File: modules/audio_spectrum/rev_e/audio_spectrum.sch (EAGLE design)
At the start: 110 parts, among them J1 AUDIO-JACK-VERTICAL, J2 SIGNPOST_DEBUG_HEADER, J3 SIGNPOST_MODULE_HEADER, J4 TC2030-JLINK-L, P1 4k-200k, P2 4k-200k, Q1 NX3008PBK, Q2 NX3008PBK, U1 AT45DB641EUDFN, U10 TLV62130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

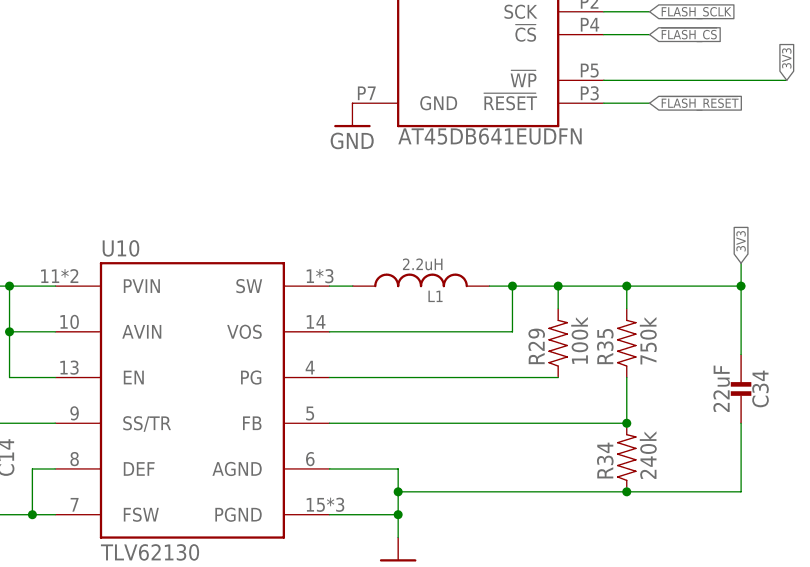
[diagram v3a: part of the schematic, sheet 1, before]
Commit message: added MPN, new BOM
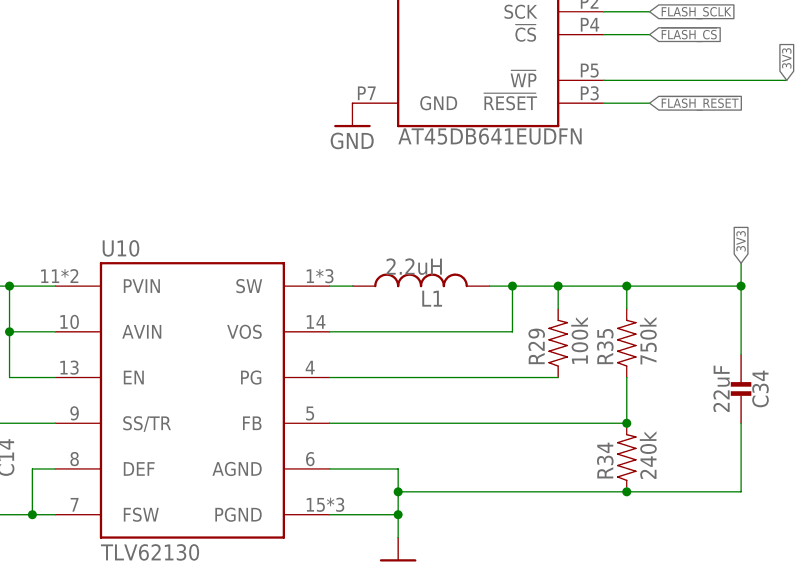
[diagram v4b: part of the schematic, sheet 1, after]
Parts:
- C1, C2: MANUFACTURER (none) -> Murata; MPN (none) -> GRM1555C1H8R0BA01D
- C10, C11, C9: MANUFACTURER (none) -> Murata; MPN (none) -> GRM188R71H102KA01D
- C12, C13: MANUFACTURER (none) -> Murata; MPN (none) -> GCM1885C1H122JA16D
- C14: MANUFACTURER (none) -> Murata; MPN (none) -> GRM188R71H332KA01D
- C15, C16, C17, C18, C19, C21, C22, C23, C24: MANUFACTURER (none) -> Murata; MPN (none) -> GRM188R71C104KA01D
- C20: MANUFACTURER (none) -> Murata; MPN (none) -> GRM155R71A104JA01D
- C25, C26, C27, C28, C29: MANUFACTURER (none) -> Murata; MPN (none) -> GRM188R61C105KA93D
- C3, C4: MANUFACTURER (none) -> Murata; MPN (none) -> GRM1885C1H330JA01D
- C30, C31: MANUFACTURER (none) -> Murata; MPN (none) -> GRM188R60J475KE19D
- C32: MANUFACTURER (none) -> TDk; MPN (none) -> C1608X5R1A685K080AC
- C33: MANUFACTURER (none) -> Murata; MPN (none) -> GRM188R60J106ME47J
- C34: MANUFACTURER (none) -> Murata; MPN (none) -> GRM186R60J226ME15D
- C5, C6: MANUFACTURER (none) -> Murata; MPN (none) -> GRM1885C1H101JA01D
- C7, C8: MANUFACTURER (none) -> Murata; MPN (none) -> GRM1885C1H361JA01D
- FB1: MANUFACTURER (none) -> Murata; MPN (none) -> BLM18HE152SN1D
- J1: MANUFACTURER (none) -> Kycon; MPN (none) -> STX-3790-5N
- L2: MANUFACTURER (none) -> Murata; MPN (none) -> LQH3NPN220MJ0L
- LED1, LED3: MANUFACTURER (none) -> Lite-On; MPN (none) -> LTST-C191KGKT
- LED2, LED4: MANUFACTURER (none) -> Lite-On; MPN (none) -> LTST-C191KRKT
- R1: MANUFACTURER (none) -> Samsung; MPN (none) -> RC1005F103CS
- R10, R11, R12, R13, R14: MANUFACTURER (none) -> Rohm; MPN (none) -> MCR03EZPFX1002
- R15, R16: MANUFACTURER (none) -> Rohm; MPN (none) -> MCR03ERTF1912
- R17, R18, R19, R20, R21, R22, R23, R24: MANUFACTURER (none) -> Rohm; MPN (none) -> MCR03ERTJ203
- R2, R3, R4, R5: MANUFACTURER (none) -> Murata; MPN (none) -> ESR03EZPJ102
- R25: MANUFACTURER (none) -> Rohm; MPN (none) -> MCR03ERTF6042
- R26, R27, R28, R29, R30, R31: MANUFACTURER (none) -> Rohm; MPN (none) -> MCR03ERTJ104
- R32, R33: MANUFACTURER (none) -> Rohm; MPN (none) -> MCR03ERTF2003
- R34: MANUFACTURER (none) -> Rohm; MPN (none) -> RHM240KCFCT-ND
- R35: MANUFACTURER (none) -> Rohm; MPN (none) -> MCR03ERTF7503
- R6, R7, R8, R9: MANUFACTURER (none) -> Rohm; MPN (none) -> MCR03ERTJ152

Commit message: changed data, added advref
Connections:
- net N$32: now also U9.ADVREFP
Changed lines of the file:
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@@
 <attribute name="DIGIKEY" value="RHM1.5KCGCT-ND"/>
 <attribute name="MANUFACTURER" value="Rohm"/>
-<attribute name="MPN" value="MCR03ERTJ152
-"/>
+<attribute name="MPN" value="MCR03ERTJ152 "/>
 </part>
 <part name="C30" library="passives" deviceset="CAPACITOR" device="0603_CAP" value="4.7uF">
@@
 <attribute name="DIGIKEY" value="RHM1.5KCGCT-ND"/>
 <attribute name="MANUFACTURER" value="Rohm"/>
-<attribute name="MPN" value="MCR03ERTJ152
-"/>
+<attribute name="MPN" value="MCR03ERTJ152 "/>
 </part>
 <part name="C31" library="passives" deviceset="CAPACITOR" device="0603_CAP" value="4.7uF">
@@
 <wire x1="119.38" y1="157.48" x2="91.44" y2="157.48" width="0.1524" layer="91"/>
 <junction x="91.44" y="157.48"/>
+<pinref part="U9" gate="U1" pin="ADVREFP"/>
+<wire x1="129.54" y1="139.7" x2="119.38" y2="139.7" width="0.1524" layer="91"/>
+<wire x1="119.38" y1="139.7" x2="119.38" y2="142.24" width="0.1524" layer="91"/>
+<junction x="119.38" y="142.24"/>
 </segment>
 </net>

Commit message: added final audio files
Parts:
- R1: value 0 -> DNP - 0
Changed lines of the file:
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@@
 <part name="GND13" library="umich" deviceset="GND" device=""/>
 <part name="GND14" library="umich" deviceset="GND" device=""/>
-<part name="R1" library="passives" deviceset="RESISTOR" device="0603_RES" value="0">
+<part name="R1" library="passives" deviceset="RESISTOR" device="0603_RES" value="DNP - 0">
 <attribute name="DIGIKEY" value="1276-3431-1-ND"/>
 <attribute name="MANUFACTURER" value="Samsung"/>
